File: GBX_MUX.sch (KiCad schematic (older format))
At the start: 26 parts, among them SW4 SW_DIPTRONICS_DHA-04TQ, U44 PI3DBS12212AZBSEX, U45 PI3DBS12212AZBSEX, U46 PI3DBS12212AZBSEX, U48 PI3DBS12212AZBSEX, U49 PI3DBS12212AZBSEX, U50 PI3DBS12212AZBSEX

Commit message: routing done
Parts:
- added C377: CC0201_100NF_6.3V_10%_X5R, CAPC0603X33N, symbol Capacitors_SMD:CC0201_100NF_6.3V_10%_X5R
- added U56: 74AHC1G04GW, ICs And Semiconductors SMD:SOT65P212X110-5N, symbol Standard_Logic:74AHC1G04GW
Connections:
- wire segments 173 -> 176
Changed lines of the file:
@@
 MGT_MUX_PD
 Wire Wire Line
-	800  3550 1300 3550
+	2300 4800 1800 4800
 Text Label 800  1700 0    50   ~ 0
 MUX3_SEL
-Text Label 800  3550 0    50   ~ 0
+Text Label 2300 4800 2    50   ~ 0
 MUX3_SEL
 $Comp
@@
 MGT_MUX_PD
 Wire Wire Line
-	3900 1700 4400 1700
+	4000 1700 4500 1700
 $Comp
 L Analog_&_Interface:PI3DBS12212AZBSEX U50
@@
 MGT_MUX_PD
 Wire Wire Line
-	3900 3550 4400 3550
-Text Label 3900 1700 0    50   ~ 0
+	4000 3550 4500 3550
+Text Label 4000 1700 0    50   ~ 0
 MUX3_SEL
-Text Label 3900 3550 0    50   ~ 0
+Text Label 4000 3550 0    50   ~ 0
 MUX3_SEL
 $Comp
@@
 	0    1    1    0
 $EndComp
+$Comp
+L Standard_Logic:74AHC1G04GW U56
+U 1 1 5FE81D64
+P 1600 4600
+F 0 "U56" H 1750 4625 50  0000 C CNN
+F 1 "74AHC1G04GW" H 1600 4165 50  0001 L CNN
+F 2 "ICs And Semiconductors SMD:SOT65P212X110-5N" H 1600 4090 50  0001 L CNN
+F 3 " " H 1600 4015 50  0001 L CNN
+F 4 "74AHC1G04GW" H 1600 3940 50  0001 L CNN "Part Number"
+F 5 "741G04" H 1600 3865 50  0001 L CNN "Library Ref"
+F 6 "SchLib\\Standard Logic.SchLib" H 1600 3790 50  0001 L CNN "Library Path"
+F 7 "74AHC1G04GW" H 1600 3715 50  0001 L CNN "Comment"
+F 8 "Standard" H 1600 3640 50  0001 L CNN "Component Kind"
+F 9 "Standard" H 1600 3565 50  0001 L CNN "Component Type"
+F 10 "74AHC1G04GW" H 1600 3490 50  0001 L CNN "Device"
+F 11 "SOT353, SOT, 0.65mm Pitch, 5 pin, 1.25mm W X 2.05mm L X 1.10mm H, IPC Medium Density" H 1600 3415 50  0001 L CNN "PackageDescription"
+F 12 " " H 1600 3340 50  0001 L CNN "Status"
+F 13 "Single Inverter Buffer" H 1600 3265 50  0001 L CNN "Part Description"
+F 14 "NXP SEMICONDUCTORS" H 1600 3190 50  0001 L CNN "Manufacturer"
+F 15 "74AHC1G04GW" H 1600 3115 50  0001 L CNN "Manufacturer Part Number"
+F 16 "3" H 1600 3040 50  0001 L CNN "Pin Count"
+F 17 "SOT353" H 1600 2965 50  0001 L CNN "Case"
+F 18 "Yes" H 1600 2890 50  0001 L CNN "Mounted"
+F 19 "No" H 1600 2815 50  0001 L CNN "Socket"
+F 20 "Yes" H 1600 2740 50  0001 L CNN "SMD"
+F 21 "No" H 1600 2665 50  0001 L CNN "PressFit"
+F 22 "No" H 1600 2590 50  0001 L CNN "Sense"
+F 23 " " H 1600 2515 50  0001 L CNN "Sense Comment"
+F 24 "No" H 1600 2440 50  0001 L CNN "Bonding"
+F 25 " " H 1600 2365 50  0001 L CNN "Status Comment"
+F 26 "1.1mm" H 1600 2290 50  0001 L CNN "ComponentHeight"
+F 27 "PcbLib\\ICs And Semiconductors SMD.PcbLib" H 1600 2215 50  0001 L CNN "Footprint Path"
+F 28 "SOT65P212X110-5N" H 1600 2140 50  0001 L CNN "Footprint Ref"
+F 29 "CERN DEM JLC" H 1600 2065 50  0001 L CNN "Author"
+F 30 " " H 1600 1990 50  0001 L CNN "ComponentLink1Description"
+F 31 " " H 1600 1915 50  0001 L CNN "ComponentLink2Description"
+F 32 "03/03/10 00:00:00" H 1600 1840 50  0001 L CNN "CreateDate"
+F 33 "03/03/10 00:00:00" H 1600 1765 50  0001 L CNN "LatestRevisionDate"
+F 34 " " H 1600 1690 50  0001 L CNN "SCEM"
+F 35 "Standard Logic" H 1600 1615 50  0001 L CNN "Database Table Name"
+F 36 "ICs And Semiconductors.DbLib" H 1600 1540 50  0001 L CNN "Library Name"
+F 37 "ICs And Semiconductors SMD" H 1600 1465 50  0001 L CNN "Footprint Library"
+F 38 "This work is licensed under the Creative Commons CC-BY-SA 4.0 License. To the extent that circuit schematics that use Licensed Material can be considered to be ‘Adapted Material’, then the copyright holder waives article 3.b of the license with respect to these schematics." H 1600 1390 50  0001 L CNN "License"
+	1    1600 4600
+	-1   0    0    -1
+$EndComp
+Wire Wire Line
+	1300 3550 650  3550
+Wire Wire Line
+	650  3550 650  4800
+Wire Wire Line
+	650  4800 1100 4800
+$Comp
+L power:GND #PWR?
+U 1 1 5FEBEDF3
+P 1800 5300
+AR Path="/5BD32060/5FEBEDF3" Ref="#PWR?"  Part="1"
+AR Path="/5C16BF13/5FEBEDF3" Ref="#PWR?"  Part="1"
+AR Path="/5C907554/5FEBEDF3" Ref="#PWR?"  Part="1"
+AR Path="/5C907554/5DCA928C/5E003981/5FEBEDF3" Ref="#PWR0811"  Part="1"
+F 0 "#PWR0811" H 1800 5050 50  0001 C CNN
+F 1 "GND" H 1805 5127 50  0000 C CNN
+F 2 "" H 1800 5300 50  0001 C CNN
+F 3 "" H 1800 5300 50  0001 C CNN
+	1    1800 5300
+	1    0    0    -1
+$EndComp
+$Comp
+L power:+3V3 #PWR?
+U 1 1 5FEBEDFB
+P 1800 5000
+AR Path="/5BD32060/5FEBEDFB" Ref="#PWR?"  Part="1"
+AR Path="/5C907554/5C417BCB/5FEBEDFB" Ref="#PWR?"  Part="1"
+AR Path="/5C907554/5FEBEDFB" Ref="#PWR?"  Part="1"
+AR Path="/5C907554/5CAAC367/5FEBEDFB" Ref="#PWR?"  Part="1"
+AR Path="/5C907554/5DCA928C/5E003981/5FEBEDFB" Ref="#PWR0810"  Part="1"
+F 0 "#PWR0810" H 1800 4850 50  0001 C CNN
+F 1 "+3V3" H 1800 5150 50  0000 C CNN
+F 2 "" H 1800 5000 50  0001 C CNN
+F 3 "" H 1800 5000 50  0001 C CNN
+	1    1800 5000
+	1    0    0    -1
+$EndComp
+$Comp
+L Capacitors_SMD:CC0201_100NF_6.3V_10%_X5R C?
+U 1 1 5FEBEE26
+P 1800 5000
+AR Path="/5BCEDA59/5FEBEE26" Ref="C?"  Part="1"
+AR Path="/5C907554/5FEBEE26" Ref="C?"  Part="1"
+AR Path="/5C907554/5DCA928C/5E003981/5FEBEE26" Ref="C377"  Part="1"
+F 0 "C377" V 1904 5110 50  0000 L CNN
+F 1 "CC0201_100NF_6.3V_10%_X5R" H 1800 4740 60  0001 L CNN
+F 2 "CAPC0603X33N" H 1800 3930 60  0001 L CNN
+F 3 "\\\\cern.ch\\dfs\\Applications\\Altium\\Datasheets\\CC0201_X5R_AVX.pdf" H 1800 4560 60  0001 L CNN
+F 4 "100nF" V 1995 5110 50  0000 L CNN "~"
+F 5 "CC0201_100NF_6.3V_10%_X5R" H 1800 4470 60  0001 L CNN "Part Number"
+F 6 "Capacitor - non polarized" H 1800 4380 60  0001 L CNN "Library Ref"
+F 7 "SchLib\\Capacitors.SchLib" H 1800 4290 60  0001 L CNN "Library Path"
+F 8 "=Value" H 1800 4200 60  0001 L CNN "Comment"
+F 9 "Standard" H 1800 4110 60  0001 L CNN "Component Kind"
+F 10 "Standard" H 1800 4020 60  0001 L CNN "Component Type"
+F 11 "2.0000000000000000e+00" H 1800 3840 60  0001 L CNN "Pin Count"
+F 12 "PcbLib\\Capacitors SMD.PcbLib" H 1800 3750 60  0001 L CNN "Footprint Path"
+F 13 "CAPC0603X33N" H 1800 3660 60  0001 L CNN "Footprint Ref"
+F 14 "~~" H 1800 3570 60  0001 L CNN "PackageDescription"
+F 15 "100nF" H 1800 3480 60  0001 L CNN "Val"
+F 16 "Not Recommended" H 1800 3390 60  0001 L CNN "Status"
+F 17 "~~" H 1800 3300 60  0001 L CNN "Status Comment"
+F 18 "6.3V" H 1800 3210 60  0001 L CNN "Voltage"
+F 19 "X5R" H 1800 3120 60  0001 L CNN "TC"
+F 20 "±10%" H 1800 3030 60  0001 L CNN "Tolerance"
+F 21 "SMD Multilayer Chip Ceramic Capacitor" H 1800 2940 60  0001 L CNN "Part Description"
+F 22 "GENERIC" H 1800 2850 60  0001 L CNN "Manufacturer"
+F 23 "CC0201_100NF_6.3V_10%_X5R" H 1800 2760 60  0001 L CNN "Manufacturer Part Number"
+F 24 "0201" H 1800 2670 60  0001 L CNN "Case"
+F 25 "Yes" H 1800 2580 60  0001 L CNN "Mounted"
+F 26 "No" H 1800 2490 60  0001 L CNN "Socket"
+F 27 "Yes" H 1800 2400 60  0001 L CNN "SMD"
+F 28 "~~" H 1800 2310 60  0001 L CNN "PressFit"
+F 29 "No" H 1800 2220 60  0001 L CNN "Sense"
+F 30 "~~" H 1800 2130 60  0001 L CNN "Sense Comment"
+F 31 "~~" H 1800 2040 60  0001 L CNN "ComponentHeight"
+F 32 "AVX" H 1800 1950 60  0001 L CNN "Manufacturer1 Example"
+F 33 "02016D104KAT2A" H 1800 1860 60  0001 L CNN "Manufacturer1 Part Number"
+F 34 "0.33mm" H 1800 1770 60  0001 L CNN "Manufacturer1 ComponentHeight"
+F 35 "\\\\cern.ch\\dfs\\Applications\\Altium\\Datasheets\\CC0201_X5R_AVX.pdf" H 1800 1680 60  0001 L CNN "HelpURL"
+F 36 "CERN DEM JLC" H 1800 1590 60  0001 L CNN "Author"
+F 37 "12/03/07 00:00:00" H 1800 1500 60  0001 L CNN "CreateDate"
+F 38 "12/03/07 00:00:00" H 1800 1410 60  0001 L CNN "LatestRevisionDate"
+F 39 "Capacitors SMD" H 1800 1320 60  0001 L CNN "Library Name"
+F 40 "This work is licensed under the Creative Commons CC-BY-SA 4.0 License. To the extent that circuit schematics that use Licensed Material can be considered to be ‘Adapted Material’, then the copyright holder waives article 3.b of the license with respect to these schematics." H 1800 1230 60  0001 L CNN "License"
+	1    1800 5000
+	0    1    1    0
+$EndComp
+Connection ~ 1800 5000
+$Comp
+L power:GND #PWR?
+U 1 1 5FF0CD0E
+P 1100 5100
+AR Path="/5BD32060/5FF0CD0E" Ref="#PWR?"  Part="1"
+AR Path="/5C16BF13/5FF0CD0E" Ref="#PWR?"  Part="1"
+AR Path="/5C907554/5FF0CD0E" Ref="#PWR?"  Part="1"
+AR Path="/5C907554/5DCA928C/5E003981/5FF0CD0E" Ref="#PWR0809"  Part="1"
+F 0 "#PWR0809" H 1100 4850 50  0001 C CNN
+F 1 "GND" H 1105 4927 50  0000 C CNN
+F 2 "" H 1100 5100 50  0001 C CNN
+F 3 "" H 1100 5100 50  0001 C CNN
+	1    1100 5100
+	1    0    0    -1
+$EndComp
 $EndSCHEMATC

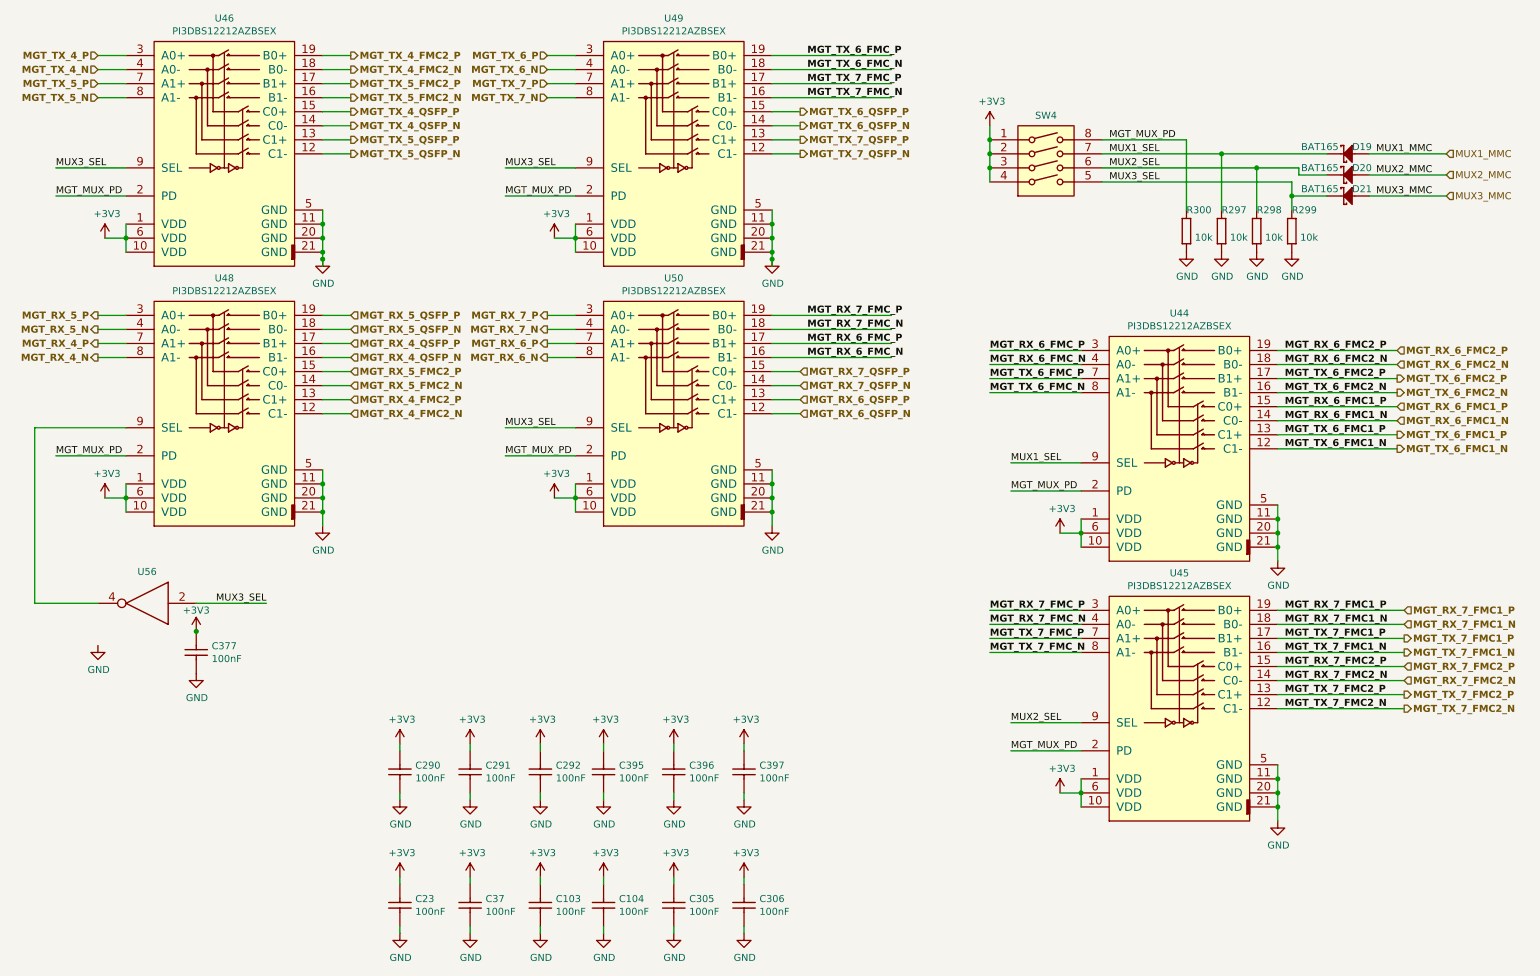
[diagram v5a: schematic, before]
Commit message: testpoints added, LEDs on the right site and other minor changes
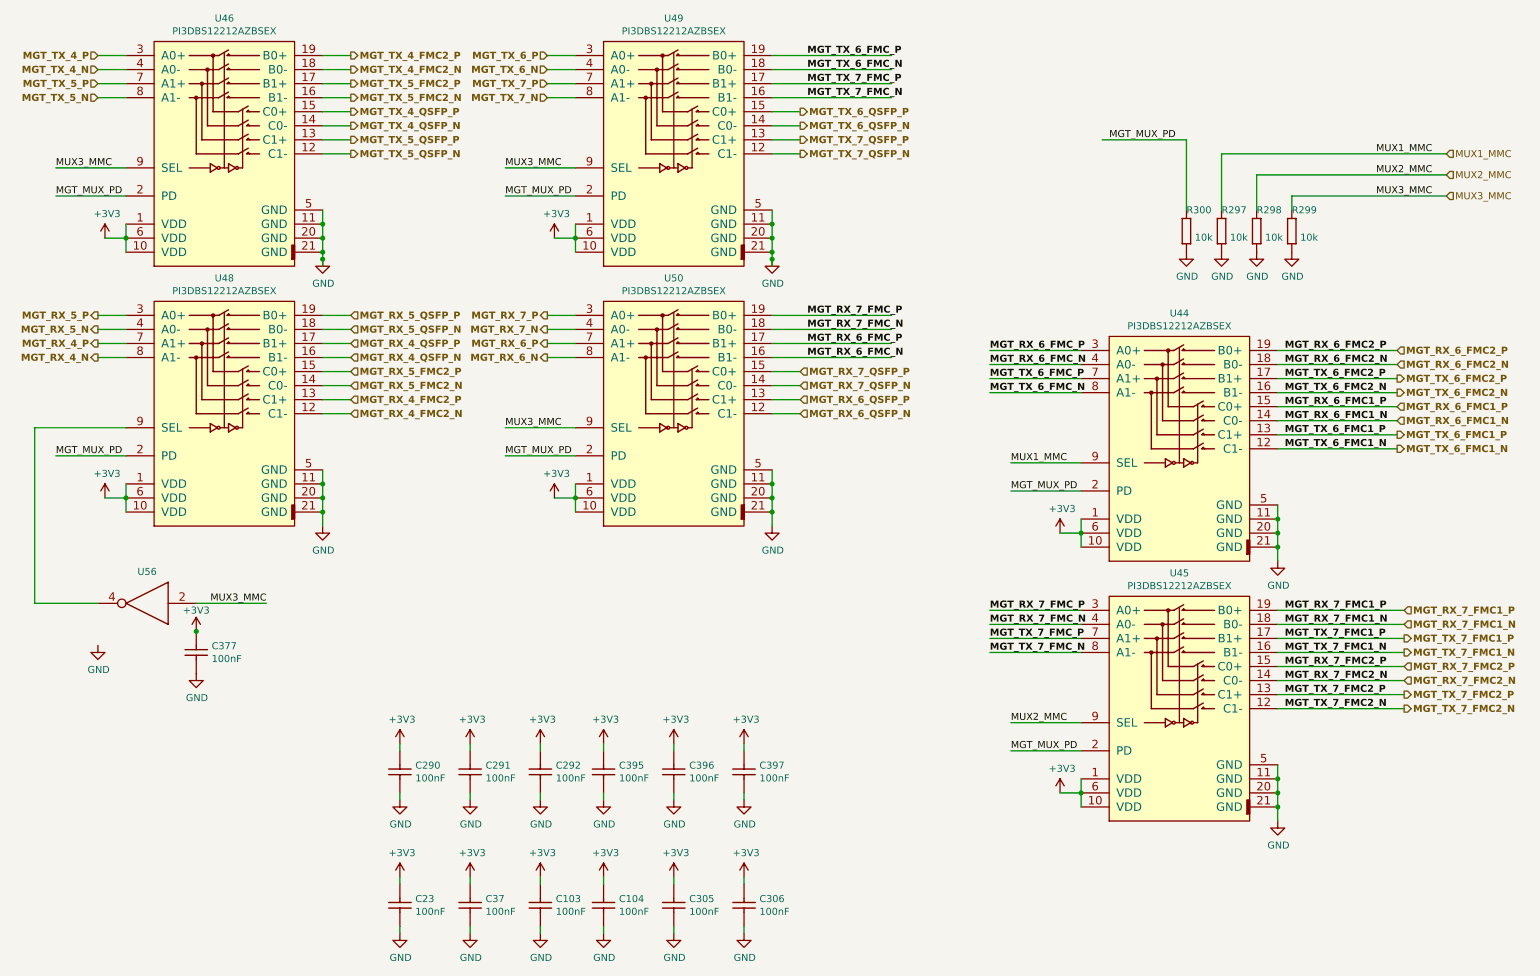
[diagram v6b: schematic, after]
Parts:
- removed D19, D20, D21: BAT165, ICs And Semiconductors SMD:SOD2512X110N, symbol Diodes:BAT165
- removed SW4: SW_DIPTRONICS_DHA-04TQ, Switches:SW_DIPTRONICS_DHA-04TQ, symbol Switches:SW_DIPTRONICS_DHA-04TQ
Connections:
- net labels removed: MUX1_SEL, MUX2_SEL, MUX3_SEL
- wire segments 176 -> 163

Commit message: Stop saying that 2-pin devices have "2.0000000000000000e+00" pins
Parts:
- C103, C104, C23, C290, C291, C292, C305, C306, C37, C377, C395, C396, C397: Pin Count 2.0000000000000000e+00 -> 2
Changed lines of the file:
@@
 F 9 "Standard" H 4700 4960 60  0001 L CNN "Component Kind"
 F 10 "Standard" H 4700 4870 60  0001 L CNN "Component Type"
-F 11 "2.0000000000000000e+00" H 4700 4690 60  0001 L CNN "Pin Count"
+F 11 "2" H 4700 4690 60  0001 L CNN "Pin Count"
 F 12 "PcbLib\\Capacitors SMD.PcbLib" H 4700 4600 60  0001 L CNN "Footprint Path"
 F 13 "CAPC0603X33N" H 4700 4510 60  0001 L CNN "Footprint Ref"
@@
 F 9 "Standard" H 5200 4960 60  0001 L CNN "Component Kind"
 F 10 "Standard" H 5200 4870 60  0001 L CNN "Component Type"
-F 11 "2.0000000000000000e+00" H 5200 4690 60  0001 L CNN "Pin Count"
+F 11 "2" H 5200 4690 60  0001 L CNN "Pin Count"
 F 12 "PcbLib\\Capacitors SMD.PcbLib" H 5200 4600 60  0001 L CNN "Footprint Path"
 F 13 "CAPC0603X33N" H 5200 4510 60  0001 L CNN "Footprint Ref"
@@
 F 9 "Standard" H 5700 4960 60  0001 L CNN "Component Kind"
 F 10 "Standard" H 5700 4870 60  0001 L CNN "Component Type"
-F 11 "2.0000000000000000e+00" H 5700 4690 60  0001 L CNN "Pin Count"
+F 11 "2" H 5700 4690 60  0001 L CNN "Pin Count"
 F 12 "PcbLib\\Capacitors SMD.PcbLib" H 5700 4600 60  0001 L CNN "Footprint Path"
 F 13 "CAPC0603X33N" H 5700 4510 60  0001 L CNN "Footprint Ref"
@@
 F 9 "Standard" H 3250 4960 60  0001 L CNN "Component Kind"
 F 10 "Standard" H 3250 4870 60  0001 L CNN "Component Type"
-F 11 "2.0000000000000000e+00" H 3250 4690 60  0001 L CNN "Pin Count"
+F 11 "2" H 3250 4690 60  0001 L CNN "Pin Count"
 F 12 "PcbLib\\Capacitors SMD.PcbLib" H 3250 4600 60  0001 L CNN "Footprint Path"
 F 13 "CAPC0603X33N" H 3250 4510 60  0001 L CNN "Footprint Ref"
@@
 F 9 "Standard" H 3750 4960 60  0001 L CNN "Component Kind"
 F 10 "Standard" H 3750 4870 60  0001 L CNN "Component Type"
-F 11 "2.0000000000000000e+00" H 3750 4690 60  0001 L CNN "Pin Count"
+F 11 "2" H 3750 4690 60  0001 L CNN "Pin Count"
 F 12 "PcbLib\\Capacitors SMD.PcbLib" H 3750 4600 60  0001 L CNN "Footprint Path"
 F 13 "CAPC0603X33N" H 3750 4510 60  0001 L CNN "Footprint Ref"
@@
 F 9 "Standard" H 4250 4960 60  0001 L CNN "Component Kind"
 F 10 "Standard" H 4250 4870 60  0001 L CNN "Component Type"
-F 11 "2.0000000000000000e+00" H 4250 4690 60  0001 L CNN "Pin Count"
+F 11 "2" H 4250 4690 60  0001 L CNN "Pin Count"
 F 12 "PcbLib\\Capacitors SMD.PcbLib" H 4250 4600 60  0001 L CNN "Footprint Path"
 F 13 "CAPC0603X33N" H 4250 4510 60  0001 L CNN "Footprint Ref"
@@
 F 9 "Standard" H 4700 5910 60  0001 L CNN "Component Kind"
 F 10 "Standard" H 4700 5820 60  0001 L CNN "Component Type"
-F 11 "2.0000000000000000e+00" H 4700 5640 60  0001 L CNN "Pin Count"
+F 11 "2" H 4700 5640 60  0001 L CNN "Pin Count"
 F 12 "PcbLib\\Capacitors SMD.PcbLib" H 4700 5550 60  0001 L CNN "Footprint Path"
 F 13 "CAPC0603X33N" H 4700 5460 60  0001 L CNN "Footprint Ref"
@@
 F 9 "Standard" H 5200 5910 60  0001 L CNN "Component Kind"
 F 10 "Standard" H 5200 5820 60  0001 L CNN "Component Type"
-F 11 "2.0000000000000000e+00" H 5200 5640 60  0001 L CNN "Pin Count"
+F 11 "2" H 5200 5640 60  0001 L CNN "Pin Count"
 F 12 "PcbLib\\Capacitors SMD.PcbLib" H 5200 5550 60  0001 L CNN "Footprint Path"
 F 13 "CAPC0603X33N" H 5200 5460 60  0001 L CNN "Footprint Ref"
@@
 F 9 "Standard" H 5700 5910 60  0001 L CNN "Component Kind"
 F 10 "Standard" H 5700 5820 60  0001 L CNN "Component Type"
-F 11 "2.0000000000000000e+00" H 5700 5640 60  0001 L CNN "Pin Count"
+F 11 "2" H 5700 5640 60  0001 L CNN "Pin Count"
 F 12 "PcbLib\\Capacitors SMD.PcbLib" H 5700 5550 60  0001 L CNN "Footprint Path"
 F 13 "CAPC0603X33N" H 5700 5460 60  0001 L CNN "Footprint Ref"
@@
 F 9 "Standard" H 3250 5910 60  0001 L CNN "Component Kind"
 F 10 "Standard" H 3250 5820 60  0001 L CNN "Component Type"
-F 11 "2.0000000000000000e+00" H 3250 5640 60  0001 L CNN "Pin Count"
+F 11 "2" H 3250 5640 60  0001 L CNN "Pin Count"
 F 12 "PcbLib\\Capacitors SMD.PcbLib" H 3250 5550 60  0001 L CNN "Footprint Path"
 F 13 "CAPC0603X33N" H 3250 5460 60  0001 L CNN "Footprint Ref"
@@
 F 9 "Standard" H 3750 5910 60  0001 L CNN "Component Kind"
 F 10 "Standard" H 3750 5820 60  0001 L CNN "Component Type"
-F 11 "2.0000000000000000e+00" H 3750 5640 60  0001 L CNN "Pin Count"
+F 11 "2" H 3750 5640 60  0001 L CNN "Pin Count"
 F 12 "PcbLib\\Capacitors SMD.PcbLib" H 3750 5550 60  0001 L CNN "Footprint Path"
 F 13 "CAPC0603X33N" H 3750 5460 60  0001 L CNN "Footprint Ref"
@@
 F 9 "Standard" H 4250 5910 60  0001 L CNN "Component Kind"
 F 10 "Standard" H 4250 5820 60  0001 L CNN "Component Type"
-F 11 "2.0000000000000000e+00" H 4250 5640 60  0001 L CNN "Pin Count"
+F 11 "2" H 4250 5640 60  0001 L CNN "Pin Count"
 F 12 "PcbLib\\Capacitors SMD.PcbLib" H 4250 5550 60  0001 L CNN "Footprint Path"
 F 13 "CAPC0603X33N" H 4250 5460 60  0001 L CNN "Footprint Ref"
@@
 F 9 "Standard" H 1800 4110 60  0001 L CNN "Component Kind"
 F 10 "Standard" H 1800 4020 60  0001 L CNN "Component Type"
-F 11 "2.0000000000000000e+00" H 1800 3840 60  0001 L CNN "Pin Count"
+F 11 "2" H 1800 3840 60  0001 L CNN "Pin Count"
 F 12 "PcbLib\\Capacitors SMD.PcbLib" H 1800 3750 60  0001 L CNN "Footprint Path"
 F 13 "CAPC0603X33N" H 1800 3660 60  0001 L CNN "Footprint Ref"

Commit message: Convert "~" and "~~" in .sch and .lib files to " "
cf. commit ef029e49 in Marble-Mini, May 21 2020
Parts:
- C103, C104, C23, C290, C291, C292, C305, C306, C37, C377, C395, C396, C397: ComponentHeight ~~ -> (none); PackageDescription ~~ -> (none); PressFit ~~ -> (none); Sense Comment ~~ -> (none); Status Comment ~~ -> (none)
- R297, R298, R299, R300: ComponentHeight ~~ -> (none); PackageDescription ~~ -> (none); Sense Comment ~~ -> (none); Status Comment ~~ -> (none); Voltage ~~ -> (none)
